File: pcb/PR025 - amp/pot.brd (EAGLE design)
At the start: 40.6 x 44.4 mm, 29 parts, among them IC1 LM317, IC2 LM337

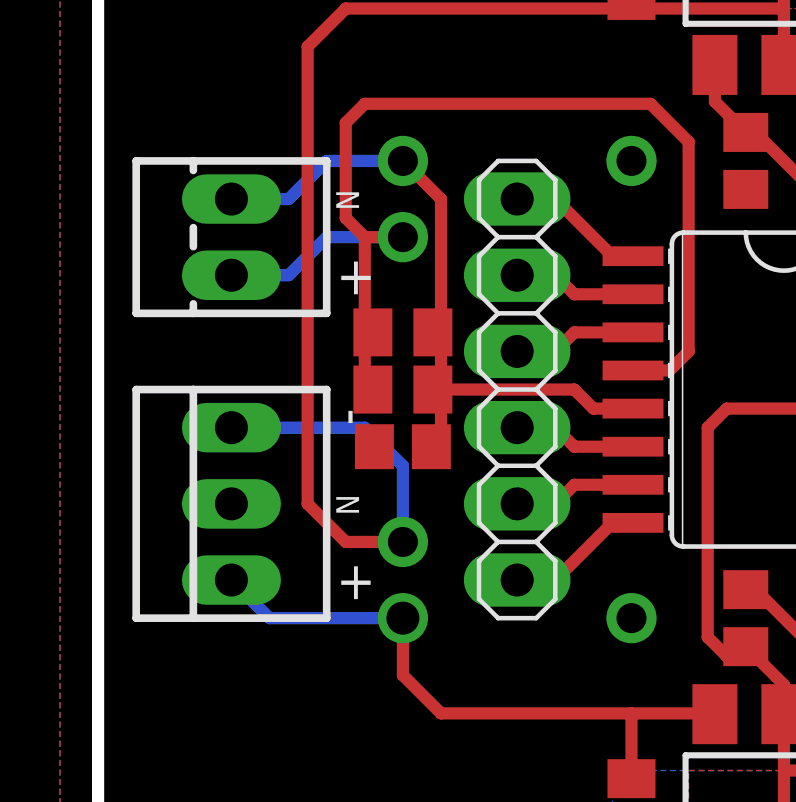
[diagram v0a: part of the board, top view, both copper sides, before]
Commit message: 
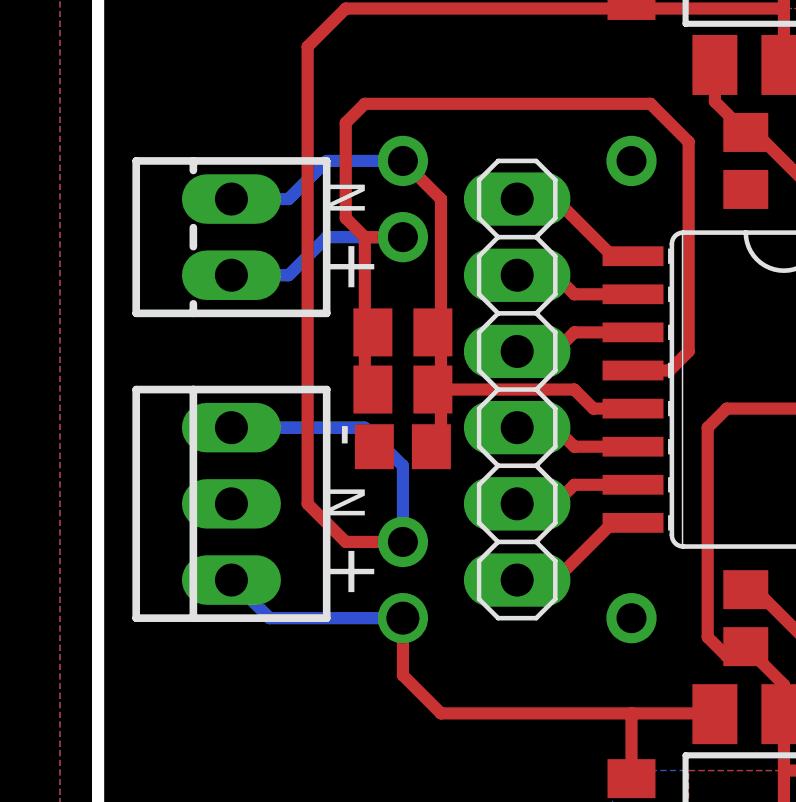
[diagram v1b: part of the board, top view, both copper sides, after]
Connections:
- net N$10 renamed SDO
- net N$11 renamed SCLK
- net N$6 renamed ZCEN
- net N$7 renamed /CS
- net N$8 renamed SDI
- net N$9 renamed /MUTE
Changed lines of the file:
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@@
 <wire x1="30.48" y1="34.29" x2="26.67" y2="30.48" width="0.4064" layer="25"/>
 <wire x1="26.67" y1="30.48" x2="26.67" y2="27.94" width="0.4064" layer="25"/>
-<text x="7.9375" y="24.765" size="1.27" layer="25" font="vector" ratio="10">+</text>
-<text x="7.9375" y="14.605" size="1.27" layer="25" font="vector" ratio="10">+</text>
-<text x="7.9375" y="18.0975" size="0.762" layer="25" font="vector" ratio="20" rot="R270">N</text>
-<text x="7.62" y="20.955" size="1.27" layer="25" font="vector" ratio="10" rot="R270">-</text>
-<text x="7.9375" y="28.2575" size="0.762" layer="25" font="vector" ratio="20" rot="R270">N</text>
+<text x="9.2075" y="24.765" size="1.778" layer="25" font="vector" ratio="20" rot="R90">+</text>
+<text x="9.2075" y="14.605" size="1.778" layer="25" font="vector" ratio="20" rot="R90">+</text>
+<text x="7.62" y="18.415" size="1.27" layer="25" font="vector" ratio="20" rot="R270">N</text>
+<text x="8.89" y="19.685" size="1.778" layer="25" font="vector" ratio="20" rot="R90">-</text>
+<text x="7.62" y="28.575" size="1.27" layer="25" font="vector" ratio="20" rot="R270">N</text>
 </plain>
 <attributes>
@@
 <wire x1="8.89" y1="20.32" x2="10.16" y2="19.05" width="0.4064" layer="16"/>
 <wire x1="10.16" y1="19.05" x2="10.16" y2="16.51" width="0.4064" layer="16"/>
-<polygon width="0.4064" layer="1">
+<polygon width="0.4064" layer="1" orphans="yes" thermals="no">
 <vertex x="26.035" y="34.29"/>
 <vertex x="26.035" y="38.1"/>
@@
 <wire x1="20.955" y1="12.7" x2="21.27" y2="12.7" width="0.4064" layer="1"/>
 <wire x1="21.27" y1="12.7" x2="21.59" y2="13.02" width="0.4064" layer="1"/>
-<polygon width="0.4064" layer="1" isolate="0.4064">
+<polygon width="0.4064" layer="1" isolate="0.4064" orphans="yes" thermals="no">
 <vertex x="19.685" y="8.89"/>
 <vertex x="26.035" y="8.89"/>
@@
 <wire x1="6.35" y1="27.94" x2="4.445" y2="27.94" width="0.4064" layer="16"/>
 </signal>
-<signal name="N$6">
+<signal name="ZCEN">
 <contactref element="U1" pad="1"/>
 <contactref element="JP1" pad="1"/>
@@
 <wire x1="15.24" y1="27.94" x2="13.97" y2="27.94" width="0.4064" layer="1"/>
 </signal>
-<signal name="N$7">
+<signal name="/CS">
 <contactref element="U1" pad="2"/>
 <contactref element="JP1" pad="2"/>
@@
 <wire x1="15.24" y1="25.4" x2="13.97" y2="25.4" width="0.4064" layer="1"/>
 </signal>
-<signal name="N$8">
+<signal name="SDI">
 <contactref element="U1" pad="3"/>
 <contactref element="JP1" pad="3"/>
@@
 <wire x1="15.24" y1="22.86" x2="13.97" y2="22.86" width="0.4064" layer="1"/>
 </signal>
-<signal name="N$9">
+<signal name="/MUTE">
 <contactref element="U1" pad="8"/>
 <contactref element="JP1" pad="6"/>
@@
 <wire x1="15.24" y1="15.24" x2="13.97" y2="15.24" width="0.4064" layer="1"/>
 </signal>
-<signal name="N$10">
+<signal name="SDO">
 <contactref element="U1" pad="7"/>
 <contactref element="JP1" pad="5"/>
@@
 <wire x1="15.24" y1="17.78" x2="13.97" y2="17.78" width="0.4064" layer="1"/>
 </signal>
-<signal name="N$11">
+<signal name="SCLK">
 <contactref element="U1" pad="6"/>
 <contactref element="JP1" pad="4"/>

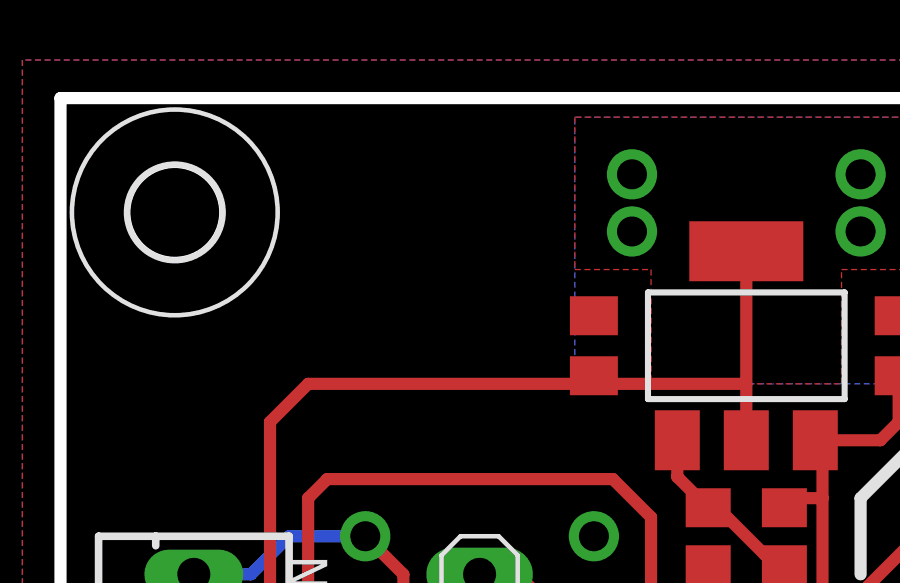
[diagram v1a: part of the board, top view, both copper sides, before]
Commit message: 
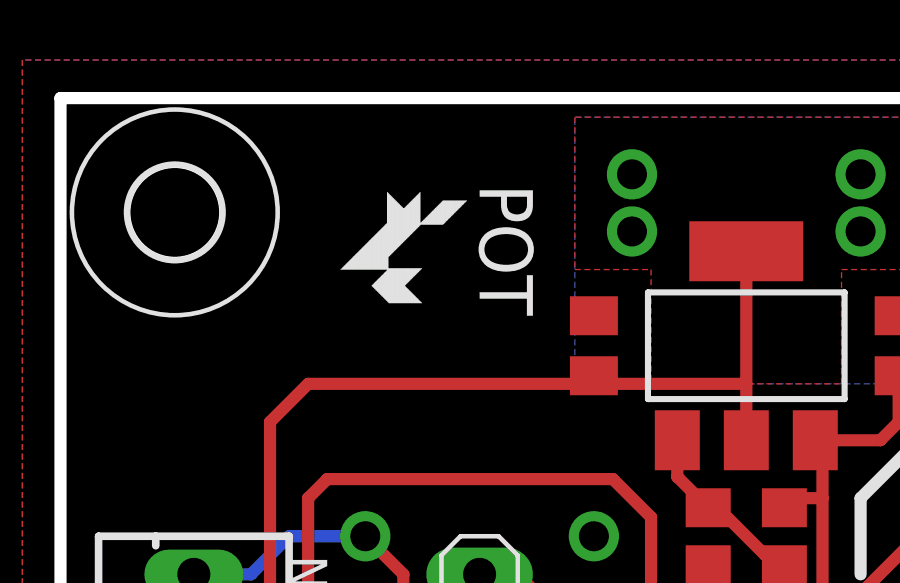
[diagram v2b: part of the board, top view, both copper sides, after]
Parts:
- added U$5: (no value), amp:FOX-1
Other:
- board text added: "POT"
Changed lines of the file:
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@@
 <text x="8.89" y="19.685" size="1.778" layer="25" font="vector" ratio="20" rot="R90">-</text>
 <text x="7.62" y="28.575" size="1.27" layer="25" font="vector" ratio="20" rot="R270">N</text>
+<text x="13.97" y="40.9575" size="1.778" layer="25" ratio="14" rot="SR270">POT</text>
 </plain>
 <attributes>
@@
 <attribute name="VALUE" x="10.795" y="29.21" size="1.27" layer="27" rot="R270"/>
 </element>
+<element name="U$5" library="amp" package="FOX-1" value="" x="11.43" y="38.735" rot="R270"/>
 </elements>
 <signals>

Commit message: 
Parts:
- C1, C2: value (none) -> 1uF
- C10: value (none) -> 100nF
- C3, C4, C9: value (none) -> 10uF
- R1, R2: value (none) -> 680
- R3, R4: value (none) -> 220
- R5: value (none) -> 0
- U1: value (none) -> PGA2311
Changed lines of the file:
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@@
 <element name="U$3" library="amp" package="3,0" value="" x="36.83" y="40.005" smashed="yes"/>
 <element name="U$4" library="amp" package="3,0" value="" x="36.83" y="3.175" smashed="yes"/>
-<element name="U1" library="amp" package="SO16W" value="" x="22.86" y="21.59" smashed="yes" rot="R270">
-<attribute name="VALUE" x="22.098" y="24.892" size="1.27" layer="27" ratio="10" rot="R270"/>
-</element>
+<element name="U1" library="amp" package="SO16W" value="PGA2311" x="22.86" y="21.59" smashed="yes" rot="R270"/>
 <element name="C5" library="amp" package="C0805K" value="100nF" x="31.115" y="19.05" smashed="yes" rot="R270"/>
 <element name="C6" library="amp" package="C0805K" value="10uF" x="33.02" y="19.05" smashed="yes" rot="R270"/>
@@
 <element name="IC1" library="amp" package="SOT223" value="LM317" x="22.86" y="7.62" smashed="yes" rot="R180"/>
 <element name="IC2" library="amp" package="SOT223" value="LM337" x="22.86" y="35.56" smashed="yes"/>
-<element name="R3" library="amp" package="R0805" value="" x="21.59" y="13.97" smashed="yes" rot="R270">
-<attribute name="VALUE" x="19.05" y="14.605" size="1.27" layer="27" rot="R270"/>
-</element>
-<element name="R1" library="amp" package="R0805" value="" x="24.13" y="13.97" smashed="yes" rot="R270">
-<attribute name="VALUE" x="21.59" y="14.605" size="1.27" layer="27" rot="R270"/>
-</element>
-<element name="R2" library="amp" package="R0805" value="" x="21.59" y="29.21" smashed="yes" rot="R270">
-<attribute name="VALUE" x="19.05" y="29.845" size="1.27" layer="27" rot="R270"/>
-</element>
-<element name="R4" library="amp" package="R0805" value="" x="24.13" y="29.21" smashed="yes" rot="R270">
-<attribute name="VALUE" x="21.59" y="29.845" size="1.27" layer="27" rot="R270"/>
-</element>
-<element name="C1" library="amp" package="C0805K" value="" x="17.78" y="7.62" smashed="yes" rot="R270">
-<attribute name="VALUE" x="15.88" y="8.62" size="1.016" layer="27" rot="R270"/>
-</element>
-<element name="C2" library="amp" package="C0805K" value="" x="17.78" y="35.56" smashed="yes" rot="R90">
-<attribute name="VALUE" x="19.68" y="34.56" size="1.016" layer="27" rot="R90"/>
-</element>
-<element name="C4" library="amp" package="C0805K" value="" x="27.94" y="35.56" smashed="yes" rot="R90">
-<attribute name="VALUE" x="29.84" y="34.56" size="1.016" layer="27" rot="R90"/>
-</element>
-<element name="C3" library="amp" package="C0805K" value="" x="27.94" y="7.62" smashed="yes" rot="R270">
-<attribute name="VALUE" x="26.04" y="8.62" size="1.016" layer="27" rot="R270"/>
-</element>
-<element name="R5" library="amp" package="R0805" value="" x="10.16" y="19.685" smashed="yes">
+<element name="R3" library="amp" package="R0805" value="220" x="21.59" y="13.97" smashed="yes" rot="R270"/>
+<element name="R1" library="amp" package="R0805" value="680" x="24.13" y="13.97" smashed="yes" rot="R270"/>
+<element name="R2" library="amp" package="R0805" value="680" x="21.59" y="29.21" smashed="yes" rot="R270"/>
+<element name="R4" library="amp" package="R0805" value="220" x="24.13" y="29.21" smashed="yes" rot="R270"/>
+<element name="C1" library="amp" package="C0805K" value="1uF" x="17.78" y="7.62" smashed="yes" rot="R270"/>
+<element name="C2" library="amp" package="C0805K" value="1uF" x="17.78" y="35.56" smashed="yes" rot="R90"/>
+<element name="C4" library="amp" package="C0805K" value="10uF" x="27.94" y="35.56" smashed="yes" rot="R90"/>
+<element name="C3" library="amp" package="C0805K" value="10uF" x="27.94" y="7.62" smashed="yes" rot="R270"/>
+<element name="R5" library="amp" package="R0805" value="0" x="10.16" y="19.685" smashed="yes">
 <attribute name="VALUE" x="9.525" y="17.145" size="1.27" layer="27"/>
 </element>
@@
 <attribute name="VALUE" x="9.525" y="24.13" size="1.016" layer="27" ratio="10" rot="R90"/>
 </element>
-<element name="C9" library="amp" package="C0805K" value="" x="10.16" y="21.59" smashed="yes">
-<attribute name="VALUE" x="9.16" y="19.69" size="1.016" layer="27"/>
-</element>
-<element name="C10" library="amp" package="C0805K" value="" x="10.16" y="23.495" smashed="yes">
-<attribute name="VALUE" x="9.16" y="21.595" size="1.016" layer="27"/>
-</element>
+<element name="C9" library="amp" package="C0805K" value="10uF" x="10.16" y="21.59" smashed="yes"/>
+<element name="C10" library="amp" package="C0805K" value="100nF" x="10.16" y="23.495" smashed="yes"/>
 <element name="JP1" library="amp" package="1X06" value="" x="13.97" y="21.59" smashed="yes" rot="R270">
 <attribute name="VALUE" x="10.795" y="29.21" size="1.27" layer="27" rot="R270"/>
